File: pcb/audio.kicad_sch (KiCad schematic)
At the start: 15 parts, among them J3 B5B-PH-SM4-TB, U5 TLV320ADC6120IRTER

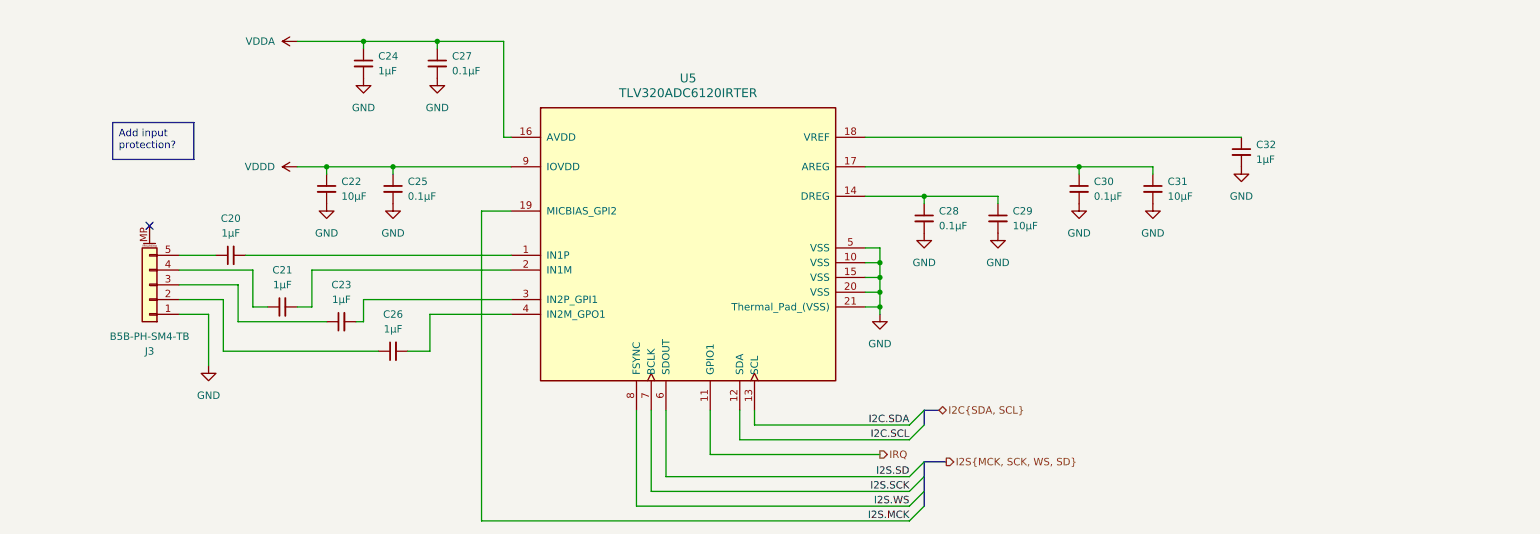
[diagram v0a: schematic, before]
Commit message: pcb: simplify power supply and define LC filter
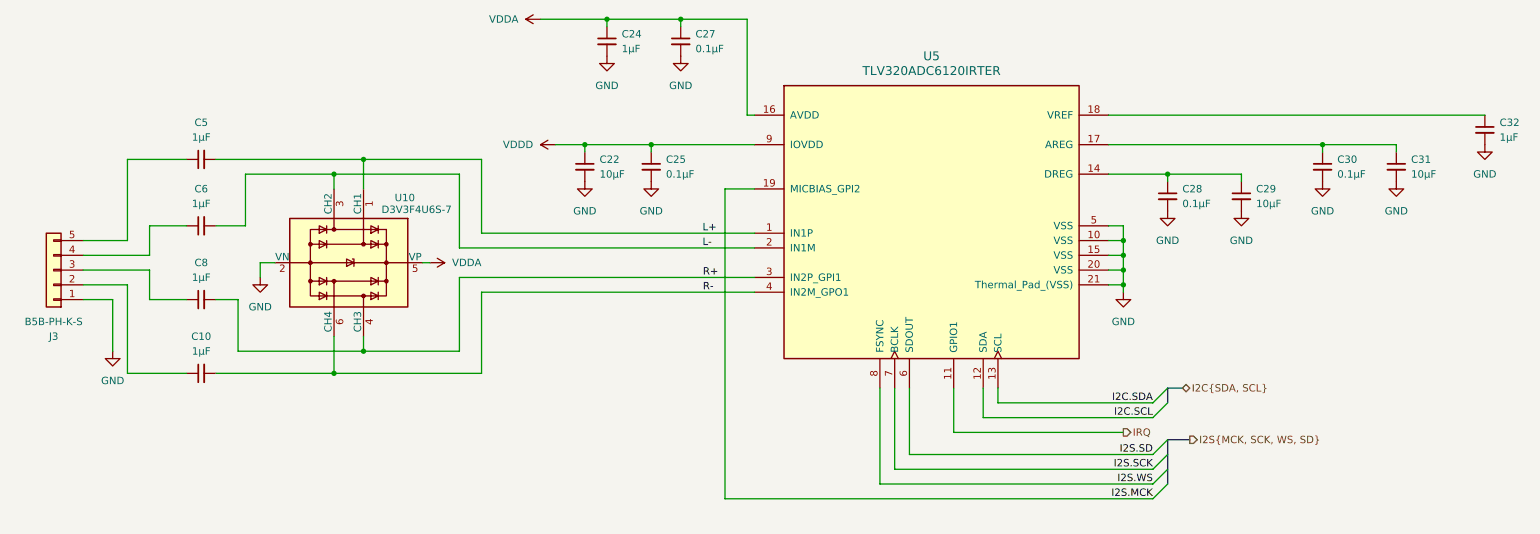
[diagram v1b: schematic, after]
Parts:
- removed C20, C21, C23, C26: 1µF, Capacitor_SMD:C_1206_3216Metric, symbol Device:C_Small
- removed J3: B5B-PH-SM4-TB, Connector_JST:JST_PH_B5B-PH-SM4-TB_1x05-1MP_P2.00mm_Vertical, symbol Connector_Generic_MountingPin:Conn_01x05_MountingPin
- added C10, C5, C6, C8: 1µF, Capacitor_SMD:C_1206_3216Metric, symbol Device:C_Small
- added J3: B5B-PH-K-S, Connector_JST:JST_PH_B5B-PH-K_1x05_P2.00mm_Vertical, symbol Connector_Generic:Conn_01x05
- added U10: D3V3F4U6S-7, Package_TO_SOT_SMD:SOT-363_SC-70-6, symbol zeus-le:D3V3F4U6S
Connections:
- net GND: now also J3.1 (Pin_1), U10.2 (VN)
- net VDDA: now also U10.5 (VP)
- net L+: now reaches U5.1 (IN1P)
- net L+: now also C5.2, U10.1 (CH1)
- net R+: now reaches U5.3 (IN2P_GPI1)
- net R+: now also C8.2, U10.4 (CH3)
- net L-: now reaches U5.2 (IN1M)
- net L-: now also C6.2, U10.3 (CH2)
- net R-: now reaches U5.4 (IN2M_GPO1)
- net R-: now also C10.2, U10.6 (CH4)
- new net: C5.1, J3.5 (Pin_5)
- new net: C6.1, J3.4 (Pin_4)
- new net: C10.1, J3.2 (Pin_2)
- new net: C8.1, J3.3 (Pin_3)
- no-connect marks 1 -> 0
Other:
- moved on the sheet: C22, C24, C25, C27, C28, C29, C30, C31, C32, U5

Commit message: pcb: pretty much the final version
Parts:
- C10, C5, C6, C8: Manufacturer Cornell Dubilier Knowles -> (none)
- C22, C29, C31: manf# (none) -> GRM188R61A106ME69D
- C24, C32: manf# (none) -> CL10B105KP8NNNC
- C25, C27, C28, C30: manf# (none) -> CL05A104KA5NNNC
- J3: manf# (none) -> B5B-PH-K-S
- U10: manf# (none) -> D3V3F4U6S-7
- U5: manf# (none) -> TLV320ADC6120IRTER
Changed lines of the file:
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@@
 			)
 		)
-		(property "Description" "Decoupling"
+		(property "Description" "Capacitor, decoupling, 25V, X5R"
+			(at 132.08 44.45 0)
+			(effects
+				(font
+					(size 1.27 1.27)
+				)
+				(hide yes)
+			)
+		)
+		(property "manf#" "CL05A104KA5NNNC"
 			(at 132.08 44.45 0)
 			(effects
@@
 			)
 		)
-		(property "Description" "Unpolarized capacitor, small symbol"
+		(property "Description" "Capacitor, decoupling, 25V, X5R"
+			(at 215.9 71.12 0)
+			(effects
+				(font
+					(size 1.27 1.27)
+				)
+				(hide yes)
+			)
+		)
+		(property "manf#" "CL05A104KA5NNNC"
 			(at 215.9 71.12 0)
 			(effects
@@
 			)
 		)
-		(property "Description" "Unpolarized capacitor, small symbol"
+		(property "Description" "Capacitor, decoupling, 10V, X7R"
+			(at 270.51 59.69 0)
+			(effects
+				(font
+					(size 1.27 1.27)
+				)
+				(hide yes)
+			)
+		)
+		(property "manf#" "CL10B105KP8NNNC"
 			(at 270.51 59.69 0)
 			(effects
@@
 			)
 		)
-		(property "Description" "Unpolarized capacitor, small symbol"
+		(property "Description" "Capacitor, decoupling, 25V, X5R"
+			(at 242.57 66.04 0)
+			(effects
+				(font
+					(size 1.27 1.27)
+				)
+				(hide yes)
+			)
+		)
+		(property "manf#" "CL05A104KA5NNNC"
 			(at 242.57 66.04 0)
 			(effects
@@
 			)
 		)
-		(property "Description" "Unpolarized capacitor, small symbol"
+		(property "Description" "Capacitor, decoupling, 10V, X5R"
+			(at 228.6 71.12 0)
+			(effects
+				(font
+					(size 1.27 1.27)
+				)
+				(hide yes)
+			)
+		)
+		(property "manf#" "GRM188R61A106ME69D"
 			(at 228.6 71.12 0)
 			(effects
@@
 			)
 		)
-		(property "Manufacturer" " Cornell Dubilier Knowles"
-			(at 49.53 64.77 90)
-			(effects
-				(font
-					(size 1.27 1.27)
-				)
-				(hide yes)
-			)
-		)
 		(property "manf#" "FCA1206A105M-H3"
 			(at 49.53 64.77 90)
@@
 			)
 		)
-		(property "Description" "Decoupling"
+		(property "Description" "Capacitor, decoupling, 10V, X7R"
+			(at 119.38 44.45 0)
+			(effects
+				(font
+					(size 1.27 1.27)
+				)
+				(hide yes)
+			)
+		)
+		(property "manf#" "CL10B105KP8NNNC"
 			(at 119.38 44.45 0)
 			(effects
@@
 			)
 		)
-		(property "Description" "Unpolarized capacitor, small symbol"
+		(property "Description" "Capacitor, decoupling, 10V, X5R"
+			(at 115.57 66.04 0)
+			(effects
+				(font
+					(size 1.27 1.27)
+				)
+				(hide yes)
+			)
+		)
+		(property "manf#" "GRM188R61A106ME69D"
 			(at 115.57 66.04 0)
 			(effects
@@
 			)
 		)
-		(property "Manufacturer" " Cornell Dubilier Knowles"
-			(at 49.53 76.2 90)
-			(effects
-				(font
-					(size 1.27 1.27)
-				)
-				(hide yes)
-			)
-		)
 		(property "manf#" "FCA1206A105M-H3"
 			(at 49.53 76.2 90)
@@
 		)
 		(property "Description" "Generic connector, single row, 01x05, script generated (kicad-library-utils/schlib/autogen/connector/)"
+			(at 24.13 83.82 0)
+			(effects
+				(font
+					(size 1.27 1.27)
+				)
+				(hide yes)
+			)
+		)
+		(property "manf#" "B5B-PH-K-S"
 			(at 24.13 83.82 0)
 			(effects
@@
 			)
 		)
-		(property "Description" "Unpolarized capacitor, small symbol"
+		(property "Description" "Capacitor, decoupling, 25V, X5R"
+			(at 127 66.04 0)
+			(effects
+				(font
+					(size 1.27 1.27)
+				)
+				(hide yes)
+			)
+		)
+		(property "manf#" "CL05A104KA5NNNC"
 			(at 127 66.04 0)
 			(effects
@@
 		)
 		(property "Description" "4 Channel Low Capacitance TVS Diode Array, SOT-363"
+			(at 74.93 82.55 0)
+			(effects
+				(font
+					(size 1.27 1.27)
+				)
+				(hide yes)
+			)
+		)
+		(property "manf#" "D3V3F4U6S-7 "
 			(at 74.93 82.55 0)
 			(effects
@@
 			)
 		)
-		(property "Description" "Unpolarized capacitor, small symbol"
+		(property "Description" "Capacitor, decoupling, 10V, X5R"
+			(at 255.27 66.04 0)
+			(effects
+				(font
+					(size 1.27 1.27)
+				)
+				(hide yes)
+			)
+		)
+		(property "manf#" "GRM188R61A106ME69D"
 			(at 255.27 66.04 0)
 			(effects
@@
 			)
 		)
-		(property "Manufacturer" " Cornell Dubilier Knowles"
-			(at 49.53 88.9 90)
-			(effects
-				(font
-					(size 1.27 1.27)
-				)
-				(hide yes)
-			)
-		)
 		(property "manf#" "FCA1206A105M-H3"
 			(at 49.53 88.9 90)
@@
 			)
 		)
-		(property "Manufacturer" " Cornell Dubilier Knowles"
-			(at 49.53 101.6 90)
-			(effects
-				(font
-					(size 1.27 1.27)
-				)
-				(hide yes)
-			)
-		)
 		(property "manf#" "FCA1206A105M-H3"
 			(at 49.53 101.6 90)
@@
 			(at 175.26 74.93 0)
 			(effects
+				(font
+					(size 1.27 1.27)
+				)
+				(hide yes)
+			)
+		)
+		(property "manf#" "TLV320ADC6120IRTER"
+			(at 175.26 74.93 0)
+			(effects

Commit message: pcb: rev 1.0 version submitted for manufacturing
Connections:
- net I2C.SCL: now also U5.13 (SCL); no longer U5.12 (SDA)
- net I2C.SDA: now also U5.12 (SDA); no longer U5.13 (SCL)
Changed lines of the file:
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@@
+		)
+	)
+	(label "I2C.SDA"
+		(at 213.36 109.22 180)
+		(fields_autoplaced yes)
+		(effects
+			(font
+				(size 1.27 1.27)
+			)
+			(justify right bottom)
 		)
 	)
@@
 		)
 	)
-	(label "I2S.WS"
-		(at 213.36 120.65 180)
+	(label "I2C.SCL"
+		(at 213.36 106.68 180)
 		(fields_autoplaced yes)
 		(effects
@@
 		)
 	)
-	(label "I2C.SCL"
-		(at 213.36 109.22 180)
+	(label "I2S.WS"
+		(at 213.36 120.65 180)
 		(fields_autoplaced yes)
 		(effects
@@
 		(fields_autoplaced yes)
 		(effects
-			(font
-				(size 1.27 1.27)
-			)
-			(justify right bottom)
-		)
-	)
-	(label "I2C.SDA"
-		(at 213.36 106.68 180)
-		(fields_autoplaced yes)
-		(effects
